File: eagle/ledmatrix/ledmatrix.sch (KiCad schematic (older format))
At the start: 21 parts, among them P1 CONN_01X05, Q1 BSS138, U1 74HC595, U2 74HC595, U3 74HC595

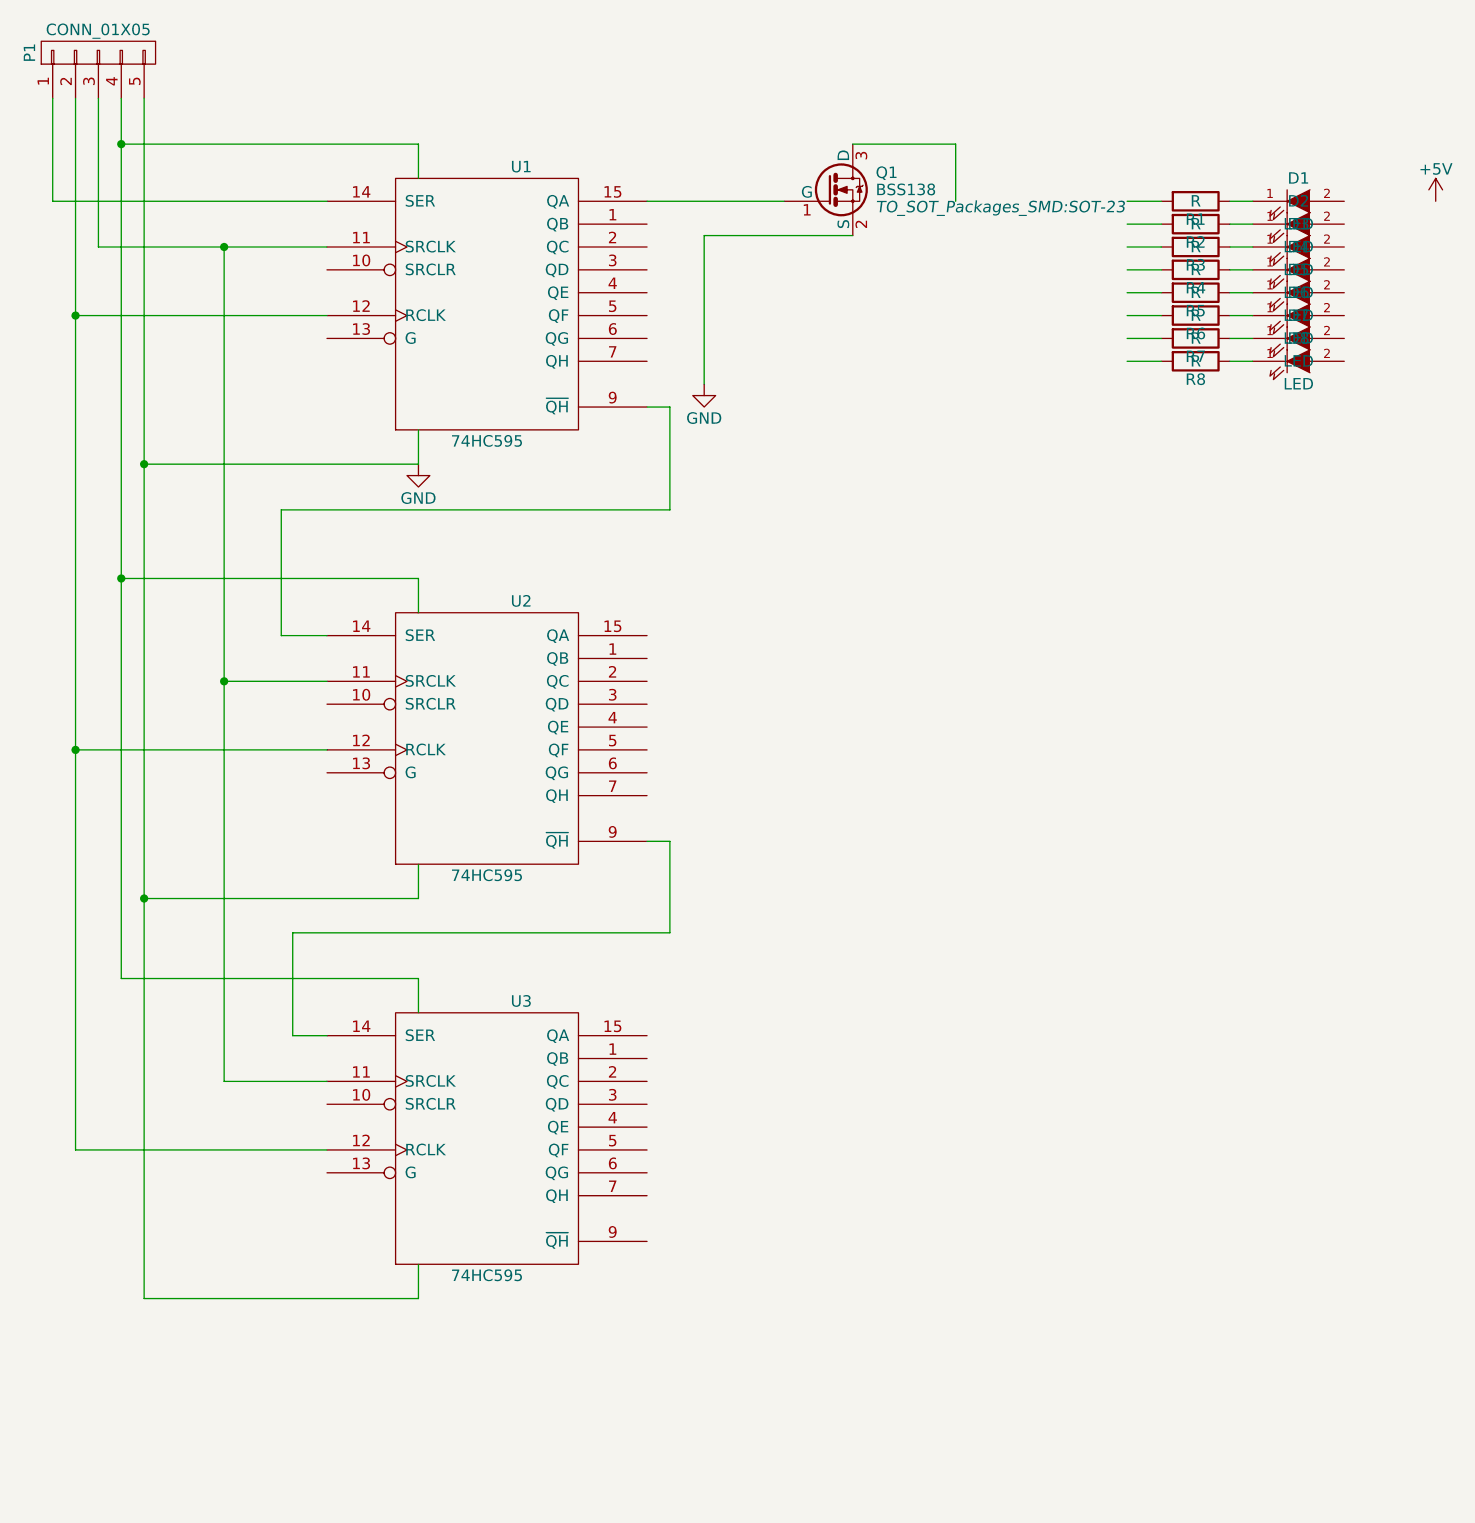
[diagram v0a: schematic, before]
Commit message: continue work on the ledmatrix schematic and board.
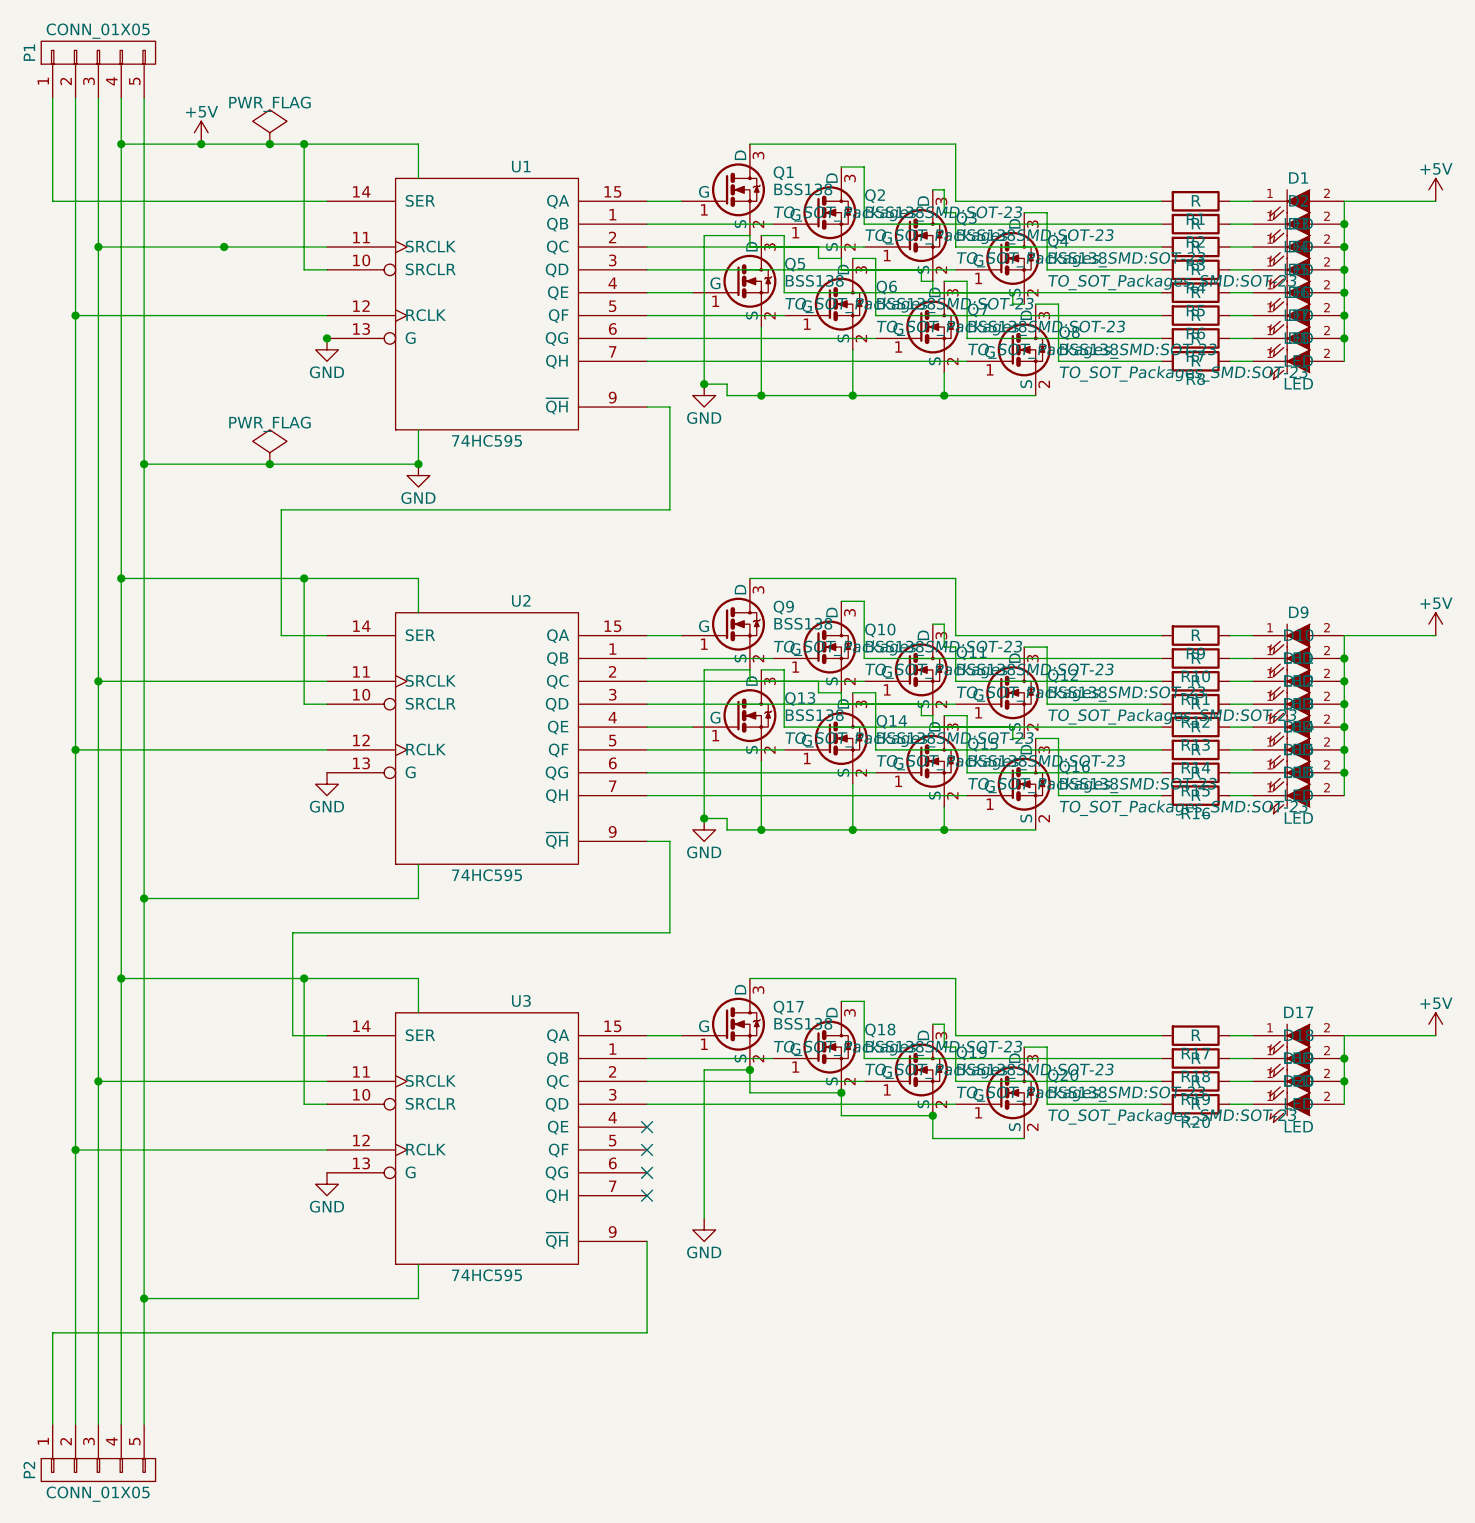
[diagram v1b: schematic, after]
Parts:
- added D10, D11, D12, D13, D14, D15, D16, D17, D18, D19, D20, D9: LED, LEDs:LED_PLCC_2835_Handsoldering, symbol LED
- added P2: CONN_01X05, Pin_Headers:Pin_Header_Straight_1x05, symbol CONN_01X05
- added Q10, Q11, Q12, Q13, Q14, Q15, Q16, Q17, Q18, Q19, Q2, Q20, Q3, Q4, Q5, Q6, Q7, Q8, Q9: BSS138, TO_SOT_Packages_SMD:SOT-23, symbol BSS138
- added R10, R11, R12, R13, R14, R15, R16, R17, R18, R19, R20, R9: R, Resistors_SMD:R_0805_HandSoldering, symbol R
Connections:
- wire segments 56 -> 203
- no-connect marks 0 -> 4
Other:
- moved on the sheet: Q1

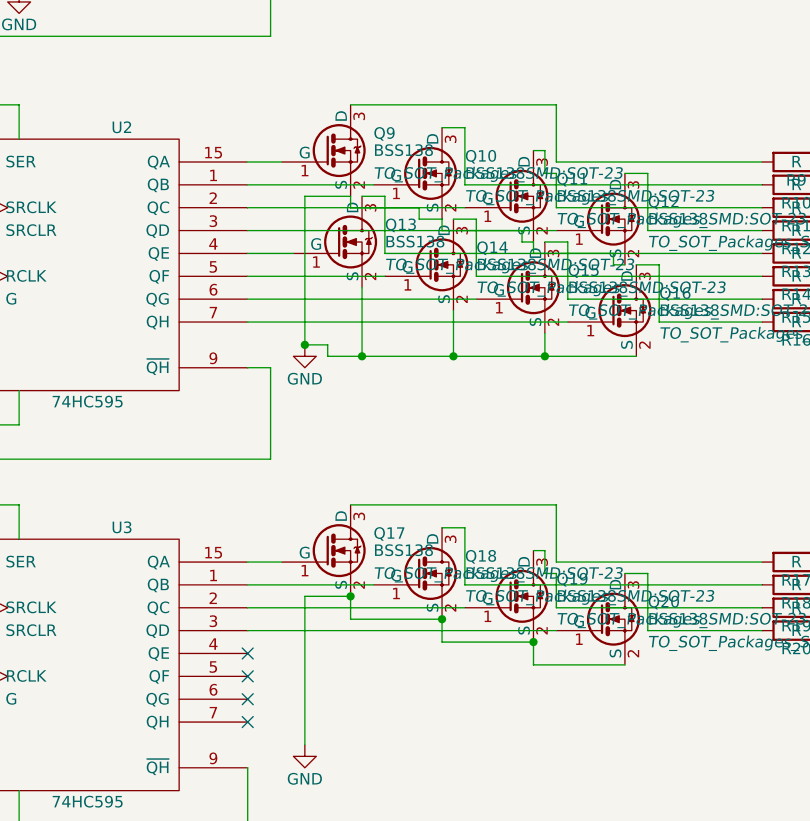
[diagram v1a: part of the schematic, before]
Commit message: layout components.
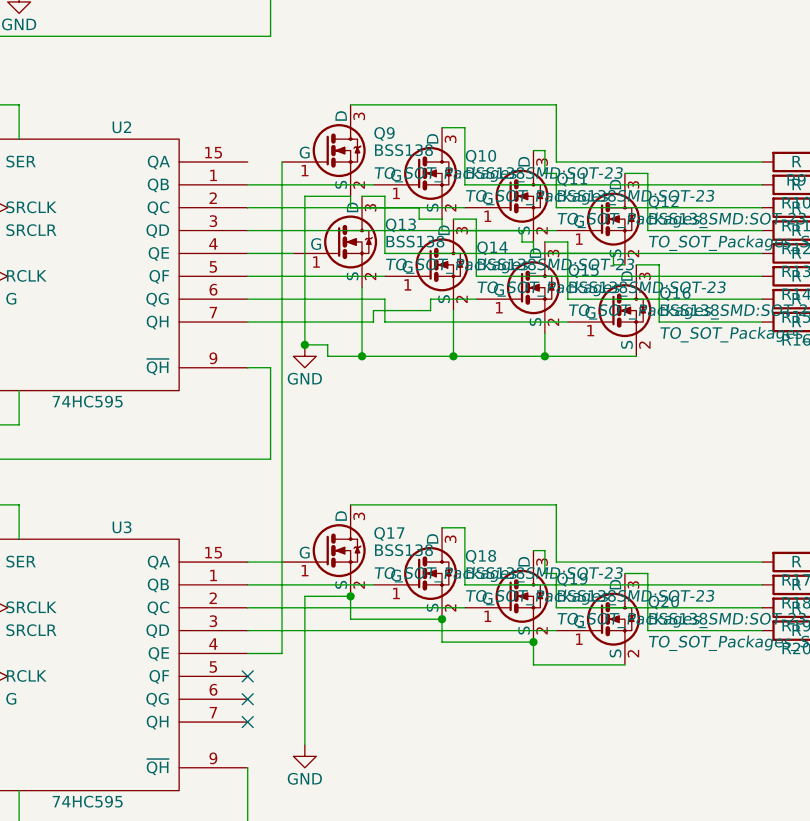
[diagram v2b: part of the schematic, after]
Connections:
- net at U2.15 (QA): no longer Q9.1 (G)
- net at U2.6 (QG): now also Q16.1 (G); no longer Q15.1 (G)
- net at U2.7 (QH): now also Q15.1 (G); no longer Q16.1 (G)
- net at U3.4 (QE): now also Q9.1 (G)
- no-connect marks 4 -> 3
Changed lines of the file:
@@
 	1    0    0    -1
 $EndComp
-Wire Wire Line
-	3950 3300 3800 3300
-$Comp
-L GND #PWR4
+$Comp
+L GND #PWR01
 U 1 1 57CDE2FE
 P 4050 2200
-F 0 "#PWR4" H 4050 1950 50  0001 C CNN
+F 0 "#PWR01" H 4050 1950 50  0001 C CNN
 F 1 "GND" H 4050 2050 50  0000 C CNN
 F 2 "" H 4050 2200 50  0000 C CNN
@@
 $EndComp
 $Comp
-L GND #PWR5
+L GND #PWR02
 U 1 1 57CDE31C
 P 2800 2550
-F 0 "#PWR5" H 2800 2300 50  0001 C CNN
+F 0 "#PWR02" H 2800 2300 50  0001 C CNN
 F 1 "GND" H 2800 2400 50  0000 C CNN
 F 2 "" H 2800 2550 50  0000 C CNN
@@
 	4250 1150 5150 1150
 $Comp
-L +5V #PWR2
+L +5V #PWR03
 U 1 1 57CDE5C8
 P 7250 1400
-F 0 "#PWR2" H 7250 1250 50  0001 C CNN
+F 0 "#PWR03" H 7250 1250 50  0001 C CNN
 F 1 "+5V" H 7250 1540 50  0000 C CNN
 F 2 "" H 7250 1400 50  0000 C CNN
@@
 Connection ~ 4050 2200
 $Comp
-L GND #PWR3
+L GND #PWR04
 U 1 1 57D0B3B9
 P 2400 2000
-F 0 "#PWR3" H 2400 1750 50  0001 C CNN
+F 0 "#PWR04" H 2400 1750 50  0001 C CNN
 F 1 "GND" H 2400 1850 50  0000 C CNN
 F 2 "" H 2400 2000 50  0000 C CNN
@@
 Connection ~ 2300 4800
 $Comp
-L GND #PWR7
+L GND #PWR05
 U 1 1 57D0C079
 P 2400 3900
-F 0 "#PWR7" H 2400 3650 50  0001 C CNN
+F 0 "#PWR05" H 2400 3650 50  0001 C CNN
 F 1 "GND" H 2400 3750 50  0000 C CNN
 F 2 "" H 2400 3900 50  0000 C CNN
@@
 $EndComp
 $Comp
-L GND #PWR10
+L GND #PWR06
 U 1 1 57D0C0D8
 P 2400 5650
-F 0 "#PWR10" H 2400 5400 50  0001 C CNN
+F 0 "#PWR06" H 2400 5400 50  0001 C CNN
 F 1 "GND" H 2400 5500 50  0000 C CNN
 F 2 "" H 2400 5650 50  0000 C CNN
@@
 	4250 4800 5150 4800
 $Comp
-L +5V #PWR9
+L +5V #PWR07
 U 1 1 57D0EB38
 P 7250 5050
-F 0 "#PWR9" H 7250 4900 50  0001 C CNN
+F 0 "#PWR07" H 7250 4900 50  0001 C CNN
 F 1 "+5V" H 7250 5190 50  0000 C CNN
 F 2 "" H 7250 5050 50  0000 C CNN
@@
 $EndComp
 $Comp
-L GND #PWR8
+L GND #PWR08
 U 1 1 57D103D0
 P 4050 4100
-F 0 "#PWR8" H 4050 3850 50  0001 C CNN
+F 0 "#PWR08" H 4050 3850 50  0001 C CNN
 F 1 "GND" H 4050 3950 50  0000 C CNN
 F 2 "" H 4050 4100 50  0000 C CNN
@@
 	4250 3050 5150 3050
 $Comp
-L +5V #PWR6
+L +5V #PWR09
 U 1 1 57D103E3
 P 7250 3300
-F 0 "#PWR6" H 7250 3150 50  0001 C CNN
+F 0 "#PWR09" H 7250 3150 50  0001 C CNN
 F 1 "+5V" H 7250 3440 50  0000 C CNN
 F 2 "" H 7250 3300 50  0000 C CNN
@@
 	3800 3700 4000 3700
 Wire Wire Line
-	3800 3800 4400 3800
-Wire Wire Line
-	3800 3900 4800 3900
-Wire Wire Line
-	3800 4000 5200 4000
-Wire Wire Line
 	4300 3450 4400 3450
 Wire Wire Line
@@
 	5050 5500 5450 5500
 $Comp
-L GND #PWR11
+L GND #PWR010
 U 1 1 57D12CB7
 P 4050 5850
-F 0 "#PWR11" H 4050 5600 50  0001 C CNN
+F 0 "#PWR010" H 4050 5600 50  0001 C CNN
 F 1 "GND" H 4050 5700 50  0000 C CNN
 F 2 "" H 4050 5850 50  0000 C CNN
@@
 Connection ~ 1600 6200
 $Comp
-L +5V #PWR1
+L +5V #PWR011
 U 1 1 57D16BE6
 P 1850 1150
-F 0 "#PWR1" H 1850 1000 50  0001 C CNN
+F 0 "#PWR011" H 1850 1000 50  0001 C CNN
 F 1 "+5V" H 1850 1290 50  0000 C CNN
 F 2 "" H 1850 1150 50  0000 C CNN
@@
 Connection ~ 2400 2000
 Connection ~ 2800 2550
-NoConn ~ 3800 5450
 NoConn ~ 3800 5550
 NoConn ~ 3800 5650
 NoConn ~ 3800 5750
 $Comp
-L PWR_FLAG #FLG1
+L PWR_FLAG #FLG012
 U 1 1 57D21391
 P 2150 1150
-F 0 "#FLG1" H 2150 1245 50  0001 C CNN
+F 0 "#FLG012" H 2150 1245 50  0001 C CNN
 F 1 "PWR_FLAG" H 2150 1330 50  0000 C CNN
 F 2 "" H 2150 1150 50  0000 C CNN
@@
 $EndComp
 $Comp
-L PWR_FLAG #FLG2
+L PWR_FLAG #FLG013
 U 1 1 57D21466
 P 2150 2550
-F 0 "#FLG2" H 2150 2645 50  0001 C CNN
+F 0 "#FLG013" H 2150 2645 50  0001 C CNN
 F 1 "PWR_FLAG" H 2150 2730 50  0000 C CNN
 F 2 "" H 2150 2550 50  0000 C CNN
@@
 Connection ~ 2150 1150
 Connection ~ 2150 2550
+Wire Wire Line
+	3950 3300 3950 5450
+Wire Wire Line
+	3950 5450 3800 5450
+Wire Wire Line
+	3800 3800 4400 3800
+Wire Wire Line
+	5200 4000 4400 4000
+Wire Wire Line
+	4400 4000 4400 3900
+Wire Wire Line
+	4400 3900 3800 3900
+Wire Wire Line
+	4800 3900 4600 3900
+Wire Wire Line
+	4600 3900 4600 3950
+Wire Wire Line
+	4600 3950 4350 3950
+Wire Wire Line
+	4350 3950 4350 4000
+Wire Wire Line
+	4350 4000 3800 4000
 $EndSCHEMATC
